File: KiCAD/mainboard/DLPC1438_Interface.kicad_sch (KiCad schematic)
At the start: 84 parts, among them IC1 DLPC1438ZEZ, IC3 SN74AUP1G06DCKR, IC4 SN74AUP1G06DCKR, IC5 SN74AUP1G06DCKR, IC6 SN74AUP1G06DCKR, IC7 SN74AUP1G06DCKR, IC8 SN74AUP1G06DCKR, J2 Conn_01x07_Pin, J3 Conn_02x05_Odd_Even, J31 Conn_01x08_Pin, J4 Conn_01x05_Pin, J7 Conn_01x05_Pin, U1 TXS0102DCU, U12 ECS-2520MV-xxx-xx, U13 MX25L3233FM2, U14 SN74AUP1G06DCKR, U22 TXS0102DCU, U5 SN74AUP1G06DCKR

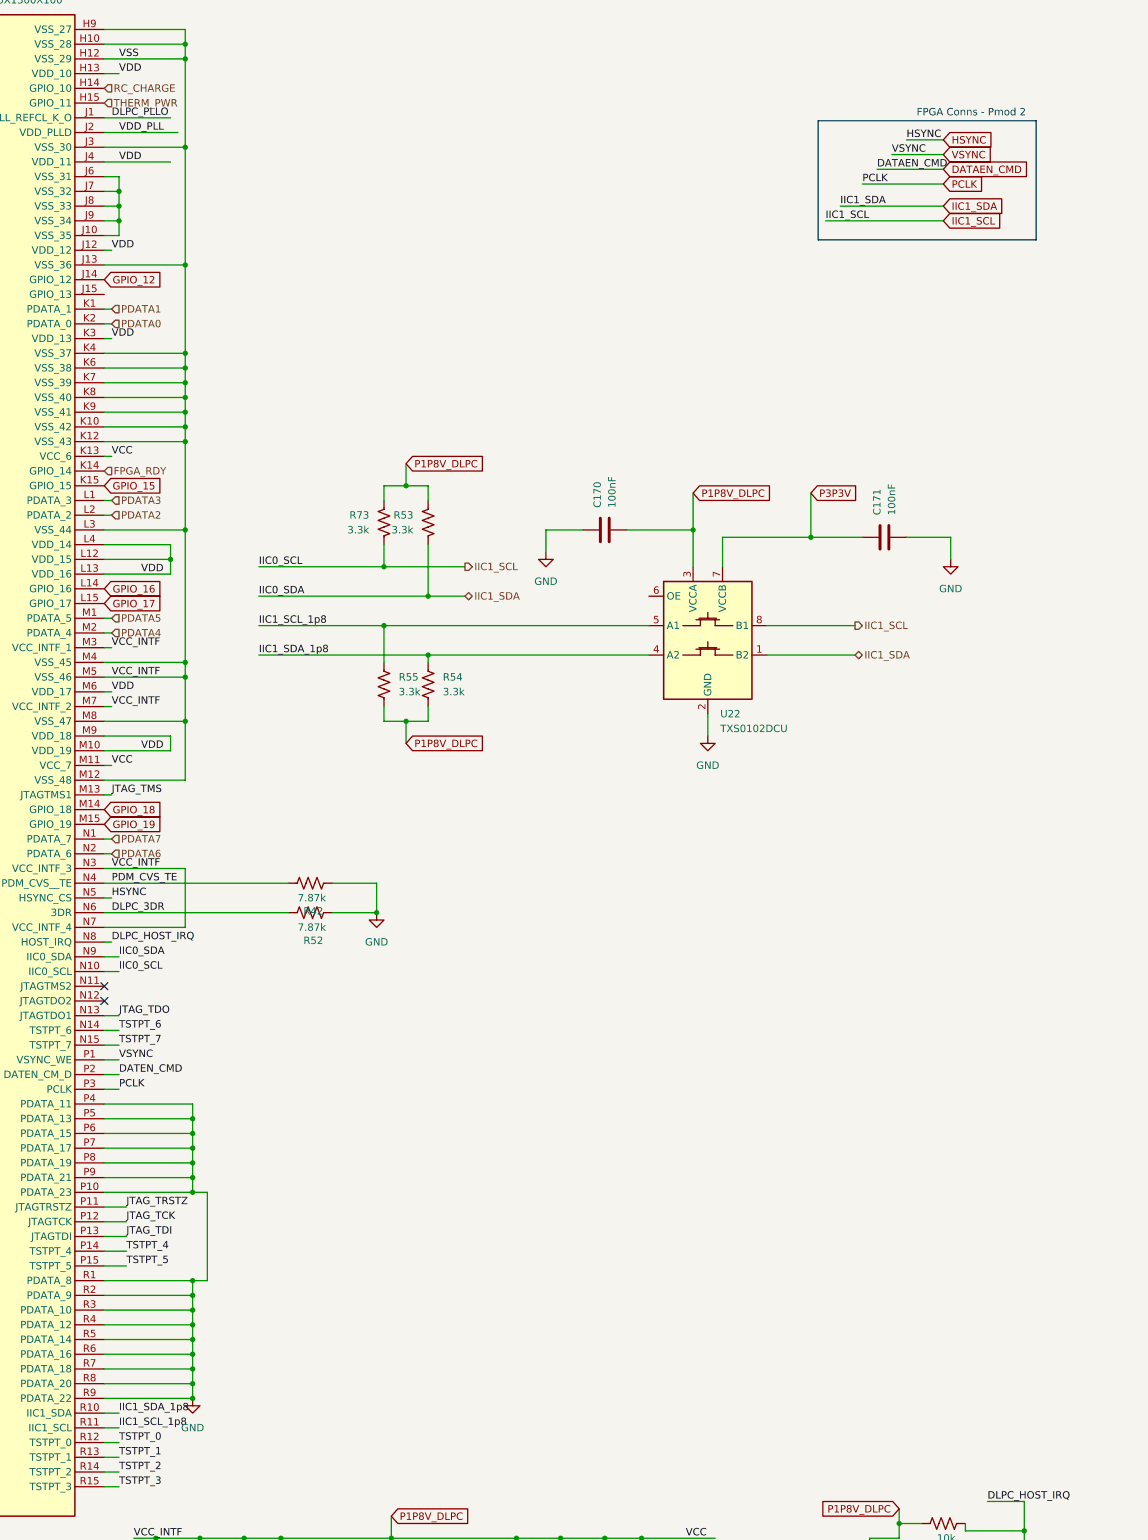
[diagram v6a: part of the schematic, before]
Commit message: fixed funny bus connectinos
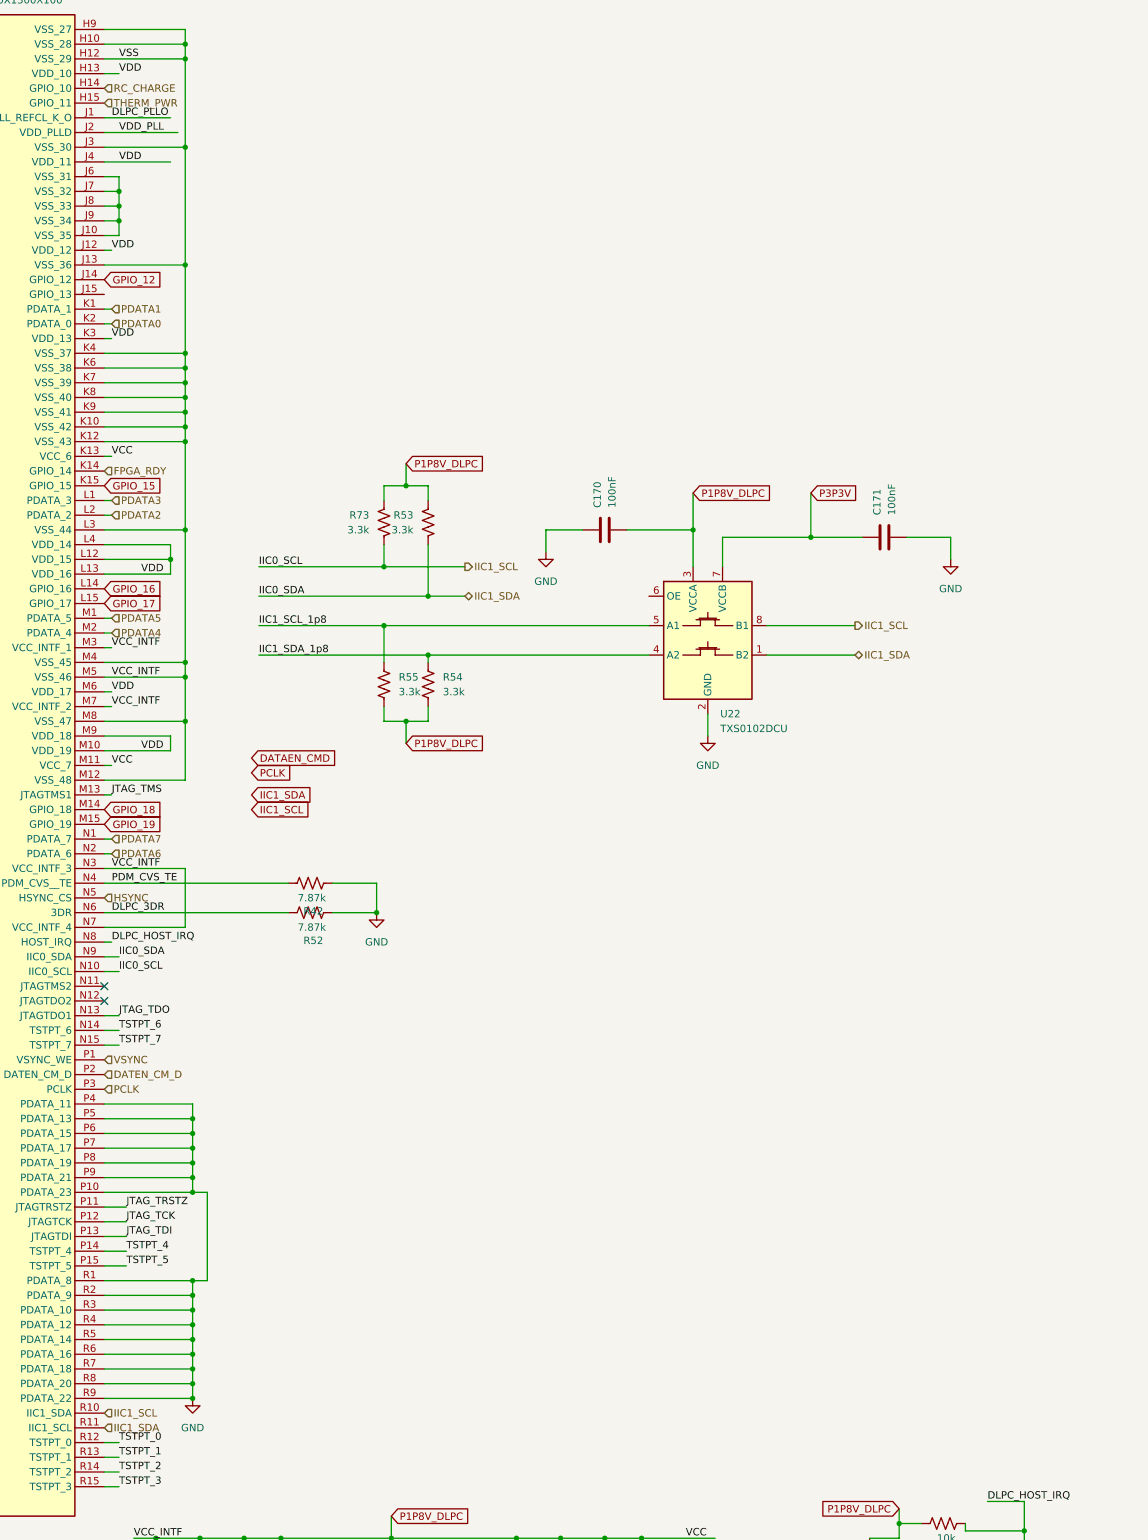
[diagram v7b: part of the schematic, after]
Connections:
- net IIC1_SCL: now also IC1.R10 (IIC1_SDA)
- net IIC1_SCL_1p8: no longer IC1.R11 (IIC1_SCL)
- net IIC1_SDA: now also IC1.R11 (IIC1_SCL)
- net IIC1_SDA_1p8: no longer IC1.R10 (IIC1_SDA)
- net DATEN_CMD renamed DATEN_CM_D
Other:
- note removed: "FPGA Conns - Pmod 2"

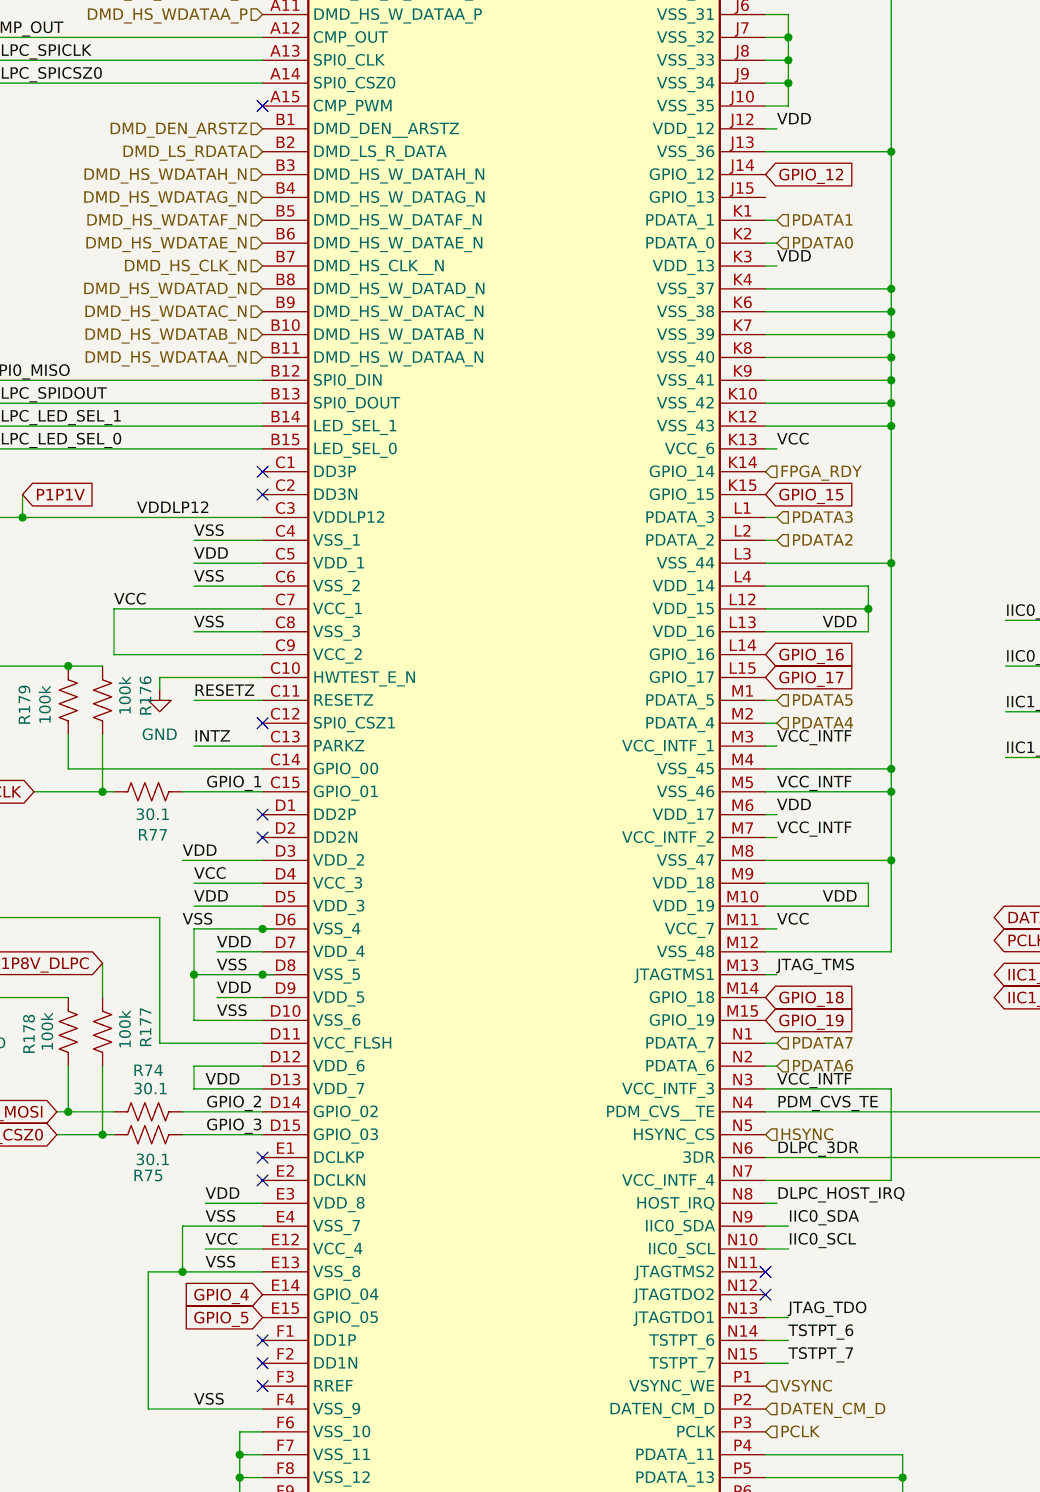
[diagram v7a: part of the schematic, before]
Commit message: gpios are now hierarchicals
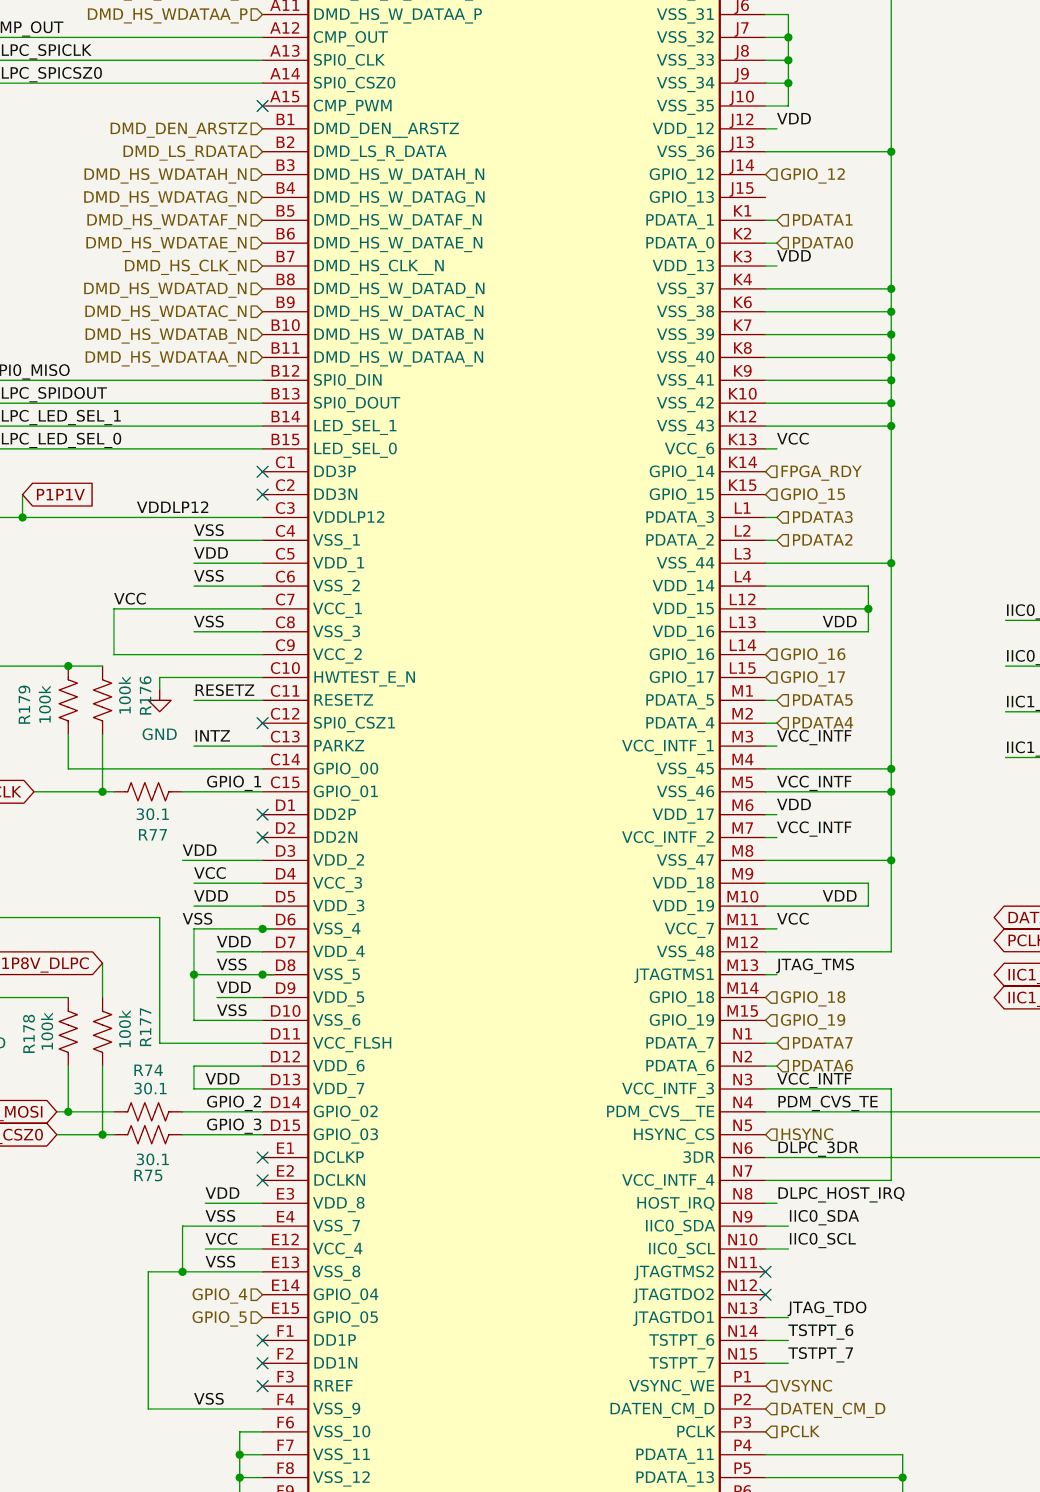
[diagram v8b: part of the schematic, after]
